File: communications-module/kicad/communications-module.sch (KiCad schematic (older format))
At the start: 3 parts

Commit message: Communications Module update
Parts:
- added P?: USB_OTG, DCP-USBCB-SC:DCP-USBCB-SC, symbol USB_OTG
- added U?: INA219, INA219:INA219, symbol INA219
- added U?: FGPMMOPA6H, FGPMMOPA6H_GPS:FGPMMOPA6H_GPS, symbol FGPMMOPA6H
- added U?: SN74LV4052A, SN74LV4052A:SN74LV4052A, symbol SN74LV4052A
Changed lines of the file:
@@
 LIBS:fgpmmopa6h_gps
 LIBS:fona_3g
+LIBS:lis3dh_breakout
+LIBS:sn74lv4052a
 LIBS:communications-module-cache
 EELAYER 25 0
@@
 Sheet 1 1
 Title "Solarcast Communications Module"
-Date "2017-01-30"
+Date "2017-01-31"
 Rev "1.0"
 Comp "Institute IRNAS Rače"
@@
 	1    0    0    -1
 $EndComp
+$Comp
+L INA219 U?
+U 1 1 5890895D
+P 7430 2175
+F 0 "U?" H 7255 2525 60  0000 C CNN
+F 1 "INA219" H 7430 1975 60  0000 C CNN
+F 2 "INA219:INA219" H 7430 1875 60  0001 C CNN
+F 3 "" H 7430 2175 60  0000 C CNN
+	1    7430 2175
+	1    0    0    -1
+$EndComp
+$Comp
+L FGPMMOPA6H U?
+U 1 1 58908AA2
+P 8685 3590
+F 0 "U?" H 8485 4090 60  0000 C CNN
+F 1 "FGPMMOPA6H" H 8685 2990 60  0000 C CNN
+F 2 "FGPMMOPA6H_GPS:FGPMMOPA6H_GPS" H 8685 2890 60  0001 C CNN
+F 3 "" H 8385 3640 60  0000 C CNN
+	1    8685 3590
+	1    0    0    -1
+$EndComp
+$Comp
+L SN74LV4052A U?
+U 1 1 58909C2A
+P 3620 2235
+F 0 "U?" H 3620 2860 60  0000 C CNN
+F 1 "SN74LV4052A" H 3620 2760 60  0000 C CNN
+F 2 "SN74LV4052A:SN74LV4052A" H 3620 1735 60  0001 C CNN
+F 3 "" H 3620 2410 60  0000 C CNN
+	1    3620 2235
+	1    0    0    -1
+$EndComp
+$Comp
+L USB_OTG P?
+U 1 1 58909E25
+P 3505 5310
+F 0 "P?" H 3830 5185 50  0000 C CNN
+F 1 "USB_OTG" H 3505 5510 50  0000 C CNN
+F 2 "DCP-USBCB-SC:DCP-USBCB-SC" H 3520 4910 60  0001 C CNN
+F 3 "" V 3455 5210 60  0000 C CNN
+	1    3505 5310
+	1    0    0    -1
+$EndComp

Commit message: Communications Module update
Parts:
- removed P?: USB_OTG, DCP-USBCB-SC:DCP-USBCB-SC, symbol USB_OTG
- removed U?: INA219, INA219:INA219, symbol INA219
- removed U?: SN74LV4052A, SN74LV4052A:SN74LV4052A, symbol SN74LV4052A
- added C? (x3): 100nF, 0603_handsolder:0603_HandSoldering, symbol C
- added C?: 1uF, 0603_handsolder:0603_HandSoldering, symbol C
- added D?: LED, 0603_handsolder:LED_0603_HandSoldering, symbol LED
- added JP? (x12): Jumper_NC_Small, symbol Jumper_NC_Small
- added L?: FERRITE, 0603_handsolder:0603_HandSoldering, symbol INDUCTOR
- added P?: USB_OTG, DCP-USBCB-SC:DCP-USBCB-SC, symbol USB_OTG
- added P? (x3): USB_A, symbol USB_A
- added R?: 1K, 0603_handsolder:0603_HandSoldering, symbol R
- added R? (x2): 10K, 0603_handsolder:0603_HandSoldering, symbol R
- added R? (x2): 0R, 0603_handsolder:0603_HandSoldering, symbol R
- added U? (x2): I2C_connector, DIP Grove 4P-2.0:DIP_Grove_4P-2_0, symbol I2C_connector
- added U?: uFL_conn, UFL-R-SMT:U.FL-R-SMT, symbol uFL_conn
- added U?: CMSIS_DAP_Breakout, symbol CMSIS_DAP_Breakout
- added U?: LIS3DH_breakout, LIS3DH_breakout:LIS3DH_breakout, symbol LIS3DH_breakout
- added U? (x2): SN74LV4052A, SN74LV4052A:SN74LV4052A, symbol SN74LV4052A
- added U?: RockBLOCK, symbol RockBLOCK
- added U?: PWR_CONN, symbol PWR_CONN
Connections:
- net labels added: +3.3V, +5V, ACC_3V3, ACC_INT1, ACC_INT2, FONA_3V3, FONA_CTS, FONA_NTWR_STAT, FONA_ON_OFF, FONA_PWR_STAT, FONA_RST, FONA_RTS, FONA_RX, FONA_TX, GEIGER0, GEIGER1, GND, GPS_3V3, GPS_BAT, GPS_RST, GPS_RX, GPS_TX, NRF_3V3, NRF_SWCLK, NRF_SWDIO, NRF_UART_CTS, NRF_UART_RTS, NRF_UART_RX, NRF_UART_TX, ROCK_5V, ROCK_CTS, ROCK_NETAV, ROCK_RTS, ROCK_RX, ROCK_TX, TWI_3V3, TWI_SCL, TWI_SDA, UART_3V3, UART_A1, UART_A2, UART_B1, UART_B2, UART_INH1, UART_INH2, VBAT
- wire segments 0 -> 71
- no-connect marks 0 -> 34
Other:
- moved on the sheet: U?

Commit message: Fixes #1
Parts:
- removed C? (x3): 100nF, 0603_handsolder:0603_HandSoldering, symbol C
- removed C?: 1uF, 0603_handsolder:0603_HandSoldering, symbol C
- removed D?: LED, 0603_handsolder:LED_0603_HandSoldering, symbol LED
- removed JP? (x12): Jumper_NC_Small, symbol Jumper_NC_Small
- removed L?: FERRITE, 0603_handsolder:0603_HandSoldering, symbol INDUCTOR
- removed P?: USB_OTG, DCP-USBCB-SC:DCP-USBCB-SC, symbol USB_OTG
- removed P? (x3): USB_A, symbol USB_A
- removed R?: 1K, 0603_handsolder:0603_HandSoldering, symbol R
- removed R? (x2): 10K, 0603_handsolder:0603_HandSoldering, symbol R
- removed R? (x2): 0R, 0603_handsolder:0603_HandSoldering, symbol R
- removed U?: nRF52832, nRF52832:nRF52832-SMD, symbol nRF52832
- removed U?: FONA_3G, FONA_3G:FONA_3G, symbol FONA_3G
- removed U?: BME280, BME280:BME280, symbol BME280
- removed U?: FGPMMOPA6H, FGPMMOPA6H_GPS:FGPMMOPA6H_GPS, symbol FGPMMOPA6H
- removed U? (x2): I2C_connector, DIP Grove 4P-2.0:DIP_Grove_4P-2_0, symbol I2C_connector
- removed U?: uFL_conn, UFL-R-SMT:U.FL-R-SMT, symbol uFL_conn
- removed U?: CMSIS_DAP_Breakout, symbol CMSIS_DAP_Breakout
- removed U?: LIS3DH_breakout, LIS3DH_breakout:LIS3DH_breakout, symbol LIS3DH_breakout
- removed U? (x2): SN74LV4052A, SN74LV4052A:SN74LV4052A, symbol SN74LV4052A
- removed U?: RockBLOCK, symbol RockBLOCK
- removed U?: PWR_CONN, symbol PWR_CONN
- added C1: 100nF, 0603_handsolder:0603_HandSoldering, symbol C
- added D1, D2: LED, 0603_handsolder:LED_0603_HandSoldering, symbol LED
- added P1: USB_OTG, DCP-USBCB-SC:DCP-USBCB-SC, symbol USB_OTG
- added R1, R2: 1K, 0603_handsolder:0603_HandSoldering, symbol R
- added R? (x2): 0R, 0603_handsolder:0603_HandSoldering, symbol R
- added U1: nRF52832, nRF52832:nRF52832-SMD, symbol nRF52832
- added U2: CMSIS_DAP_Programmer, symbol CMSIS_DAP_Breakout
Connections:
- net +3V3: now also C1.2, R?.2, R?.2, U1.18 (VIN)
- net GEIGER0: now also U1.8 (P0.28/AIN4)
- net GEIGER1: now also U1.9 (P0.29/AIN5)
- net GND: now also C1.1, D1.1 (K), D2.1 (K), P1.5 (GND), U1.19 (GND), U2.1 (GND)
- net NRF_SWCLK: now also P1.2 (D-), U1.21 (SWCLK), U2.5 (SWCLK)
- net NRF_SWDIO: now also P1.3 (D+), U1.22 (SWDIO), U2.6 (SWDIO)
- net TWI_SCL: now also U1.6 (P0.26)
- net TWI_SDA: now also U1.5 (P0.25)
- new net: R?.1, U2.2 (VCC)
- new net: P1.1 (VCC), R?.1
- new net: D1.2 (A), R1.1
- new net: D2.2 (A), R2.1
- new net ENABLE-3V3: U1.24 (NFC1/P0.09)
- new net ENABLE-5V: U1.25 (NFC2/P0.10)
- new net ENABLE-VBAT: U1.35 (P0.20)
- new net ENABLE_AIR: U1.28 (P0.13)
- new net ENABLE_CELL: U1.31 (P0.16)
- new net ENABLE_GEIG: U1.29 (P0.14)
- new net ENABLE_GPS: U1.33 (P0.18)
- new net ENABLE_LORA: U1.32 (P0.17)
- new net ENABLE_ROCK: U1.34 (P0.19)
- new net ENABLE_TWI: U1.30 (P0.15)
- new net LED_RED: R1.2, U1.3 (P0.23)
- new net LED_YEL: R2.2, U1.4 (P0.24)
- new net LIS_INT: U1.13 (AIN0/P0.02)
- new net MCU_CTS: U1.27 (P0.12)
- new net MCU_RTS: U1.26 (P0.11)
- new net MCU_RX: U1.23 (P0.08)
- new net MCU_TX: U1.20 (P0.07)
- new net SPI_CS: U1.16 (AIN3/P0.05)
- new net SPI_MISO: U1.15 (AIN2/P0.04)
- new net SPI_MOSI: U1.14 (AIN1/P0.03)
- new net SPI_SCLK: U1.17 (P0.06)
- new net UMUX_INH: U1.7 (P0.27)
- new net UMUX_SEL0: U1.1 (P0.21/nRESET)
- new net UMUX_SEL1: U1.2 (P0.22)
- no-connect marks 34 -> 8

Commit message: Communications Module update
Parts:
- U2: footprint (none) -> CMSIS_DAP_Breakout:CMSIS_DAP_Breakout
- gave numbers to parts that had none: 2
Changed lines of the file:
@@
 NoConn ~ 2120 5820
 $Comp
-L GND #PWR01
+L GND #PWR6
 U 1 1 58931E61
 P 3600 6615
-F 0 "#PWR01" H 3600 6365 50  0001 C CNN
+F 0 "#PWR6" H 3600 6365 50  0001 C CNN
 F 1 "GND" H 3600 6465 50  0000 C CNN
 F 2 "" H 3600 6615 60  0000 C CNN
@@
 $EndComp
 $Comp
-L GND #PWR02
+L GND #PWR14
 U 1 1 58931E7C
 P 7370 2205
-F 0 "#PWR02" H 7370 1955 50  0001 C CNN
+F 0 "#PWR14" H 7370 1955 50  0001 C CNN
 F 1 "GND" H 7370 2055 50  0000 C CNN
 F 2 "" H 7370 2205 60  0000 C CNN
@@
 TWI_SCL
 $Comp
-L +5V #PWR03
+L +5V #PWR18
 U 1 1 589B725B
 P 9405 2000
-F 0 "#PWR03" H 9405 1850 50  0001 C CNN
+F 0 "#PWR18" H 9405 1850 50  0001 C CNN
 F 1 "+5V" H 9405 2140 50  0000 C CNN
 F 2 "" H 9405 2000 60  0000 C CNN
@@
 $EndComp
 $Comp
-L +3.3V #PWR04
+L +3.3V #PWR17
 U 1 1 589BA386
 P 9235 2105
-F 0 "#PWR04" H 9235 1955 50  0001 C CNN
+F 0 "#PWR17" H 9235 1955 50  0001 C CNN
 F 1 "+3.3V" H 9235 2245 50  0000 C CNN
 F 2 "" H 9235 2105 60  0000 C CNN
@@
 TWI_SCL
 $Comp
-L +3.3V #PWR05
+L +3.3V #PWR1
 U 1 1 589D07BB
 P 1625 2270
-F 0 "#PWR05" H 1625 2120 50  0001 C CNN
+F 0 "#PWR1" H 1625 2120 50  0001 C CNN
 F 1 "+3.3V" H 1625 2410 50  0000 C CNN
 F 2 "" H 1625 2270 60  0000 C CNN
@@
 $EndComp
 $Comp
-L GND #PWR06
+L GND #PWR2
 U 1 1 589D089E
 P 1840 2205
-F 0 "#PWR06" H 1840 1955 50  0001 C CNN
+F 0 "#PWR2" H 1840 1955 50  0001 C CNN
 F 1 "GND" H 1840 2055 50  0000 C CNN
 F 2 "" H 1840 2205 60  0000 C CNN
@@
 F 0 "U2" H 6695 4200 60  0000 C CNN
 F 1 "CMSIS_DAP_Programmer" H 7090 3405 60  0000 C CNN
-F 2 "" H 6645 4250 60  0000 C CNN
+F 2 "CMSIS_DAP_Breakout:CMSIS_DAP_Breakout" H 7050 3295 60  0001 C CNN
 F 3 "" H 6645 4250 60  0000 C CNN
 	1    6770 3800
@@
 $EndComp
 $Comp
-L GND #PWR07
+L GND #PWR13
 U 1 1 58931E71
 P 7095 3550
-F 0 "#PWR07" H 7095 3300 50  0001 C CNN
+F 0 "#PWR13" H 7095 3300 50  0001 C CNN
 F 1 "GND" H 7095 3400 50  0000 C CNN
 F 2 "" H 7095 3550 60  0000 C CNN
@@
 NRF_SWDIO
 $Comp
-L GND #PWR08
+L GND #PWR9
 U 1 1 589F3D38
 P 4440 1430
-F 0 "#PWR08" H 4440 1180 50  0001 C CNN
+F 0 "#PWR9" H 4440 1180 50  0001 C CNN
 F 1 "GND" H 4440 1280 50  0000 C CNN
 F 2 "" H 4440 1430 60  0000 C CNN
@@
 	4440 1520 4605 1520
 $Comp
-L +3.3V #PWR09
+L +3.3V #PWR8
 U 1 1 589F526D
 P 4205 1565
-F 0 "#PWR09" H 4205 1415 50  0001 C CNN
+F 0 "#PWR8" H 4205 1415 50  0001 C CNN
 F 1 "+3.3V" H 4205 1705 50  0000 C CNN
 F 2 "" H 4205 1565 60  0000 C CNN
@@
 	4205 1750 4605 1750
 $Comp
-L +5V #PWR010
+L +5V #PWR7
 U 1 1 589F74B8
 P 4030 1740
-F 0 "#PWR010" H 4030 1590 50  0001 C CNN
+F 0 "#PWR7" H 4030 1590 50  0001 C CNN
 F 1 "+5V" H 4030 1880 50  0000 C CNN
 F 2 "" H 4030 1740 60  0000 C CNN
@@
 VBAT
 $Comp
-L GND #PWR011
+L GND #PWR16
 U 1 1 58A04074
 P 8960 4360
-F 0 "#PWR011" H 8960 4110 50  0001 C CNN
+F 0 "#PWR16" H 8960 4110 50  0001 C CNN
 F 1 "GND" H 8960 4210 50  0000 C CNN
 F 2 "" H 8960 4360 60  0000 C CNN
@@
 GEIGER1
 $Comp
-L +3.3V #PWR012
+L +3.3V #PWR5
 U 1 1 58A17094
 P 3375 6720
-F 0 "#PWR012" H 3375 6570 50  0001 C CNN
+F 0 "#PWR5" H 3375 6570 50  0001 C CNN
 F 1 "+3.3V" H 3375 6860 50  0000 C CNN
 F 2 "" H 3375 6720 60  0000 C CNN
@@
 $EndComp
 $Comp
-L GND #PWR013
+L GND #PWR3
 U 1 1 58A5FEB2
 P 2035 6480
-F 0 "#PWR013" H 2035 6230 50  0001 C CNN
+F 0 "#PWR3" H 2035 6230 50  0001 C CNN
 F 1 "GND" H 2035 6330 50  0000 C CNN
 F 2 "" H 2035 6480 60  0000 C CNN
@@
 $EndComp
 $Comp
-L +3.3V #PWR014
+L +3.3V #PWR4
 U 1 1 58A61565
 P 2335 6480
-F 0 "#PWR014" H 2335 6330 50  0001 C CNN
+F 0 "#PWR4" H 2335 6330 50  0001 C CNN
 F 1 "+3.3V" H 2335 6620 50  0000 C CNN
 F 2 "" H 2335 6480 60  0000 C CNN
@@
 $EndComp
 $Comp
-L GND #PWR015
+L GND #PWR11
 U 1 1 58A6A31B
 P 6735 5235
-F 0 "#PWR015" H 6735 4985 50  0001 C CNN
+F 0 "#PWR11" H 6735 4985 50  0001 C CNN
 F 1 "GND" H 6735 5085 50  0000 C CNN
 F 2 "" H 6735 5235 60  0000 C CNN
@@
 $EndComp
 $Comp
-L GND #PWR016
+L GND #PWR12
 U 1 1 58A6A460
 P 6740 5610
-F 0 "#PWR016" H 6740 5360 50  0001 C CNN
+F 0 "#PWR12" H 6740 5360 50  0001 C CNN
 F 1 "GND" H 6740 5460 50  0000 C CNN
 F 2 "" H 6740 5610 60  0000 C CNN
@@
 NoConn ~ 2120 5720
 $Comp
-L +3.3V #PWR?
+L +3.3V #PWR10
 U 1 1 58AF377D
 P 6610 2280
-F 0 "#PWR?" H 6610 2130 50  0001 C CNN
+F 0 "#PWR10" H 6610 2130 50  0001 C CNN
 F 1 "+3.3V" H 6610 2420 50  0000 C CNN
 F 2 "" H 6610 2280 60  0000 C CNN
@@
 $EndComp
 $Comp
-L +3.3V #PWR?
+L +3.3V #PWR15
 U 1 1 58AF6071
 P 7555 3755
-F 0 "#PWR?" H 7555 3605 50  0001 C CNN
+F 0 "#PWR15" H 7555 3605 50  0001 C CNN
 F 1 "+3.3V" H 7555 3895 50  0000 C CNN
 F 2 "" H 7555 3755 60  0000 C CNN
@@
 $EndComp
 $Comp
-L R R?
+L R R10
 U 1 1 58AF8640
 P 7405 3755
-F 0 "R?" V 7485 3755 50  0000 C CNN
+F 0 "R10" V 7485 3755 50  0000 C CNN
 F 1 "0R" V 7405 3755 50  0000 C CNN
 F 2 "0603_handsolder:0603_HandSoldering" V 7335 3755 30  0001 C CNN
@@
 $EndComp
 $Comp
-L R R?
+L R R9
 U 1 1 58AF96B6
 P 6760 2280
-F 0 "R?" V 6840 2280 50  0000 C CNN
+F 0 "R9" V 6840 2280 50  0000 C CNN
 F 1 "0R" V 6760 2280 50  0000 C CNN
 F 2 "0603_handsolder:0603_HandSoldering" V 6690 2280 30  0001 C CNN

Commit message: All gerbers update
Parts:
- removed P1: USB_OTG, DCP-USBCB-SC:DCP-USBCB-SC, symbol USB_OTG
- removed R10, R9: 0R, 0603_handsolder:0603_HandSoldering, symbol R
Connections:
- no-connect marks 8 -> 6
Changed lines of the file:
@@
 Comment4 ""
 $EndDescr
-NoConn ~ 7270 2205
 $Comp
 L nRF52832 U1
@@
 Text GLabel 2120 5220 0    60   Input ~ 0
 TWI_SCL
-$Comp
-L USB_OTG P1
-U 1 1 58931E7B
-P 7170 1905
-F 0 "P1" H 7495 1780 50  0000 C CNN
-F 1 "USB_OTG" H 7170 2105 50  0000 C CNN
-F 2 "DCP-USBCB-SC:DCP-USBCB-SC" H 7245 1325 60  0001 C CNN
-F 3 "" V 7120 1805 60  0000 C CNN
-	1    7170 1905
-	1    0    0    -1
-$EndComp
-$Comp
-L GND #PWR02
-U 1 1 58931E7C
-P 7370 2205
-F 0 "#PWR02" H 7370 1955 50  0001 C CNN
-F 1 "GND" H 7370 2055 50  0000 C CNN
-F 2 "" H 7370 2205 60  0000 C CNN
-F 3 "" H 7370 2205 60  0000 C CNN
-	1    7370 2205
-	1    0    0    -1
-$EndComp
-Text GLabel 7070 2205 3    60   Input ~ 0
-NRF_SWCLK
-Text GLabel 7170 2205 3    60   Input ~ 0
-NRF_SWDIO
-NoConn ~ 7270 2205
-NoConn ~ 7570 1805
 $Sheet
 S 9545 1980 930  3095
@@
 NoConn ~ 2120 5620
 NoConn ~ 2120 5720
-$Comp
-L +3.3V #PWR017
-U 1 1 58AF377D
-P 6610 2280
-F 0 "#PWR017" H 6610 2130 50  0001 C CNN
-F 1 "+3.3V" H 6610 2420 50  0000 C CNN
-F 2 "" H 6610 2280 60  0000 C CNN
-F 3 "" H 6610 2280 60  0000 C CNN
-	1    6610 2280
-	0    -1   -1   0
-$EndComp
-$Comp
-L +3.3V #PWR018
-U 1 1 58AF6071
-P 7555 3755
-F 0 "#PWR018" H 7555 3605 50  0001 C CNN
-F 1 "+3.3V" H 7555 3895 50  0000 C CNN
-F 2 "" H 7555 3755 60  0000 C CNN
-F 3 "" H 7555 3755 60  0000 C CNN
-	1    7555 3755
-	0    1    1    0
-$EndComp
-$Comp
-L R R10
-U 1 1 58AF8640
-P 7405 3755
-F 0 "R10" V 7485 3755 50  0000 C CNN
-F 1 "0R" V 7405 3755 50  0000 C CNN
-F 2 "0603_handsolder:0603_HandSoldering" V 7335 3755 30  0001 C CNN
-F 3 "" H 7405 3755 30  0000 C CNN
-	1    7405 3755
-	0    -1   -1   0
-$EndComp
-$Comp
-L R R9
-U 1 1 58AF96B6
-P 6760 2280
-F 0 "R9" V 6840 2280 50  0000 C CNN
-F 1 "0R" V 6760 2280 50  0000 C CNN
-F 2 "0603_handsolder:0603_HandSoldering" V 6690 2280 30  0001 C CNN
-F 3 "" H 6760 2280 30  0000 C CNN
-	1    6760 2280
-	0    1    1    0
-$EndComp
-Wire Wire Line
-	7095 3650 7180 3650
-Wire Wire Line
-	7180 3650 7180 3755
-Wire Wire Line
-	7180 3755 7255 3755
-Wire Wire Line
-	6970 2205 6970 2280
-Wire Wire Line
-	6970 2280 6910 2280
+NoConn ~ 7095 3650
 $EndSCHEMATC

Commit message: Communications Module schematic update
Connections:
- net LIS_INT renamed ACC_INT
- net MCU_CTS renamed UART_CTS
- net MCU_RTS renamed UART_RTS
- net MCU_RX renamed UART_RX
- net MCU_TX renamed UART_TX
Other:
- moved on the sheet: D1, D2, R1, R2, U2

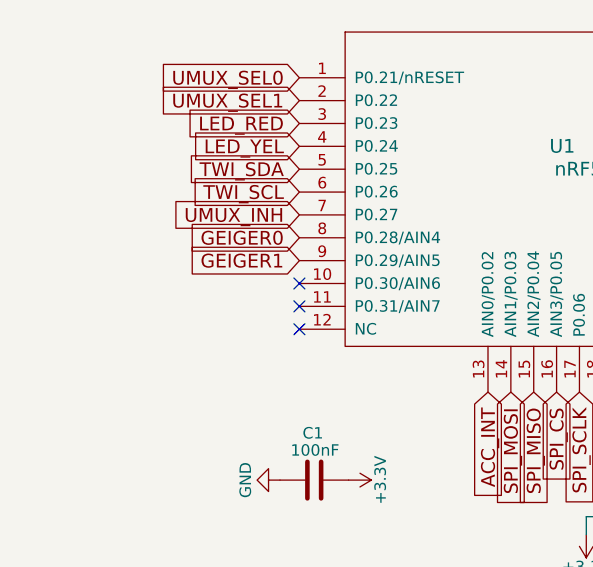
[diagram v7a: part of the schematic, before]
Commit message: Communications Module PCB components placed
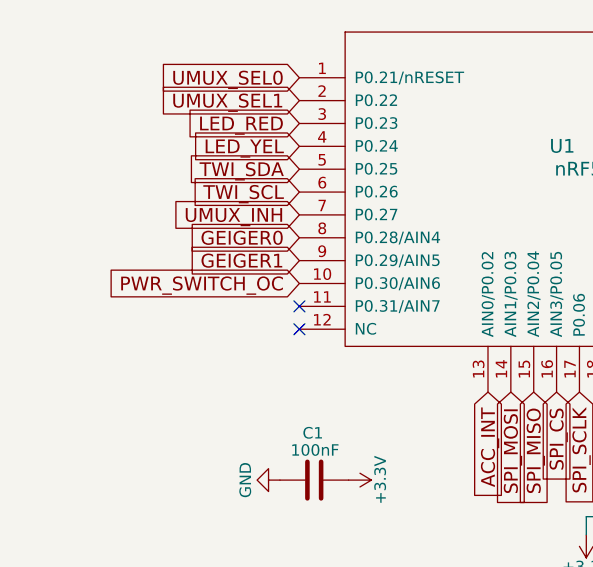
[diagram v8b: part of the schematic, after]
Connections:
- net PWR_SWITCH_OC: now also U1.10 (P0.30/AIN6)
- no-connect marks 6 -> 5
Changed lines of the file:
@@
 Text GLabel 4770 4720 2    60   Input ~ 0
 ENABLE-VBAT
-NoConn ~ 2120 5620
 NoConn ~ 2120 5720
 NoConn ~ 7240 4545
@@
 	0    1    1    0
 $EndComp
+Text GLabel 2120 5620 0    60   Input ~ 0
+PWR_SWITCH_OC
 $EndSCHEMATC
